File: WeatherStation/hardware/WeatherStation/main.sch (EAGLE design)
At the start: 38 parts, among them IC1 4017N, IC2 4017N

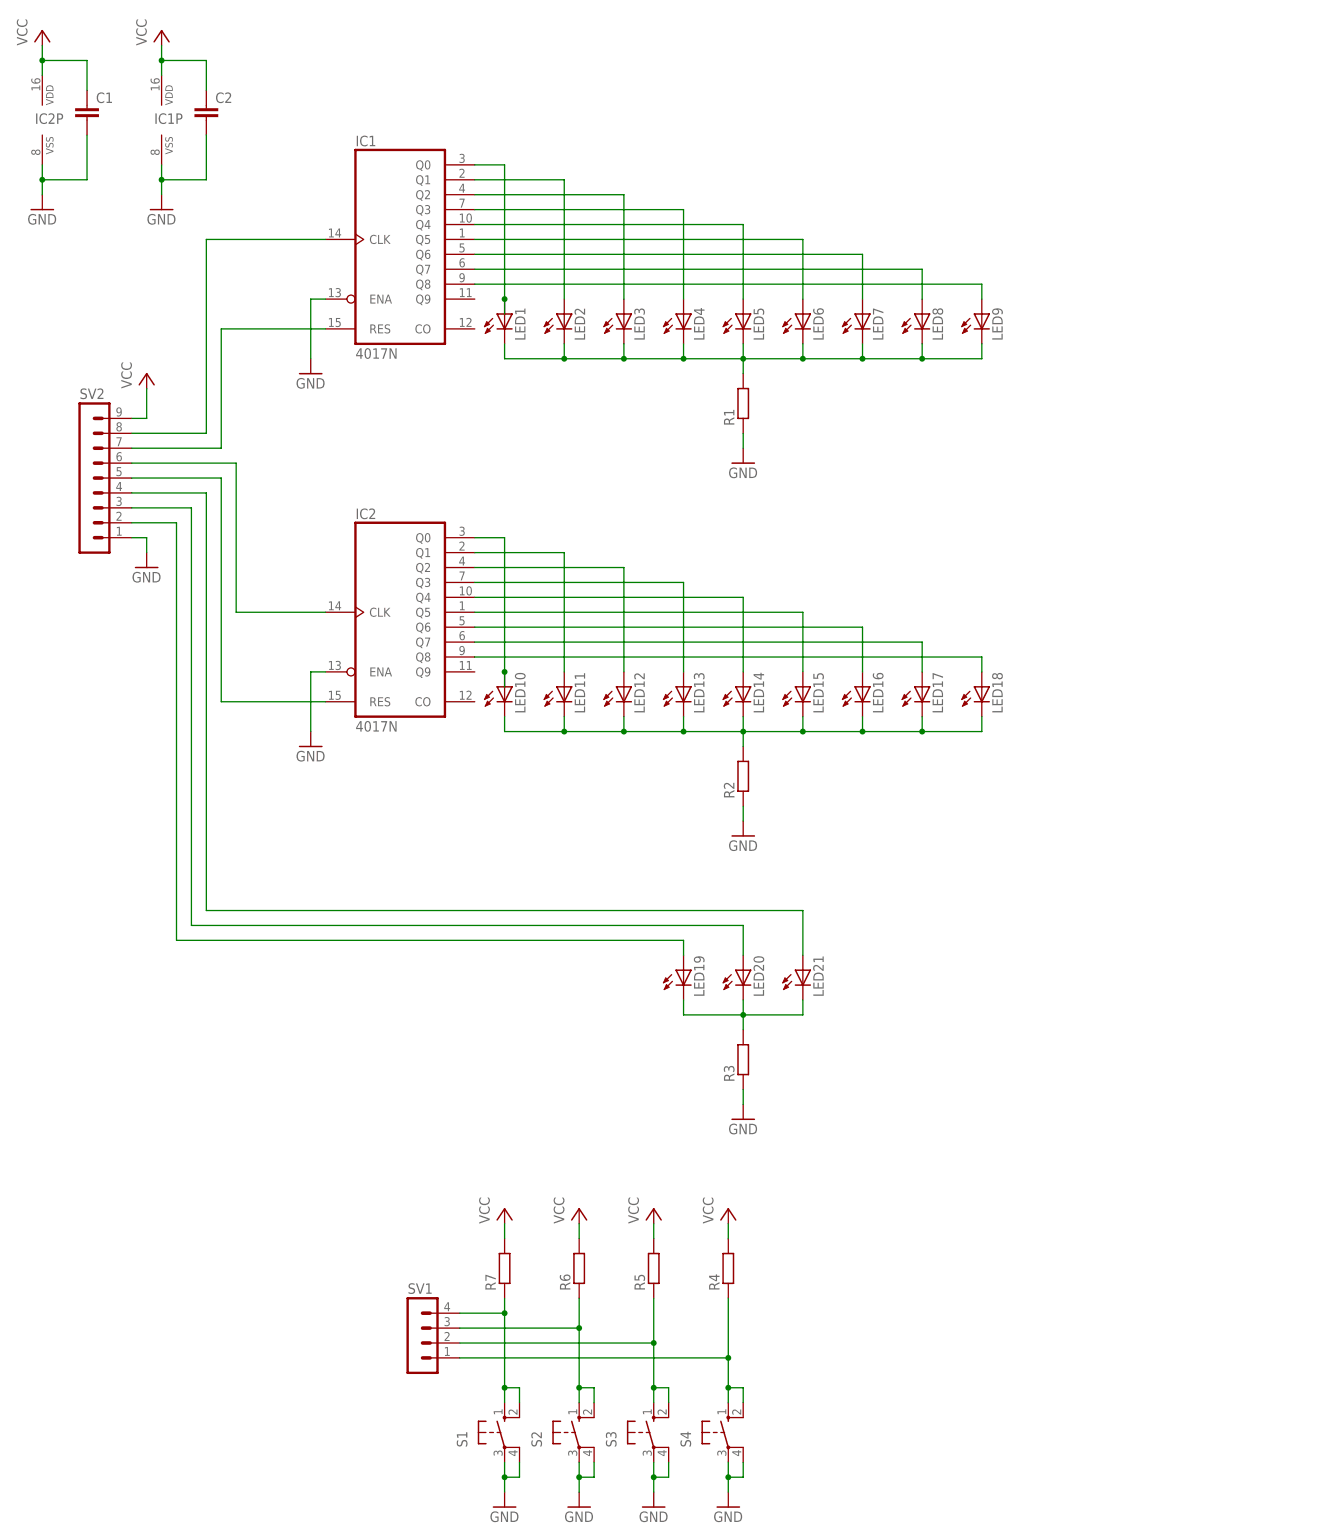
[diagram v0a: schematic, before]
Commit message: SCT2167 used as a LED driver.
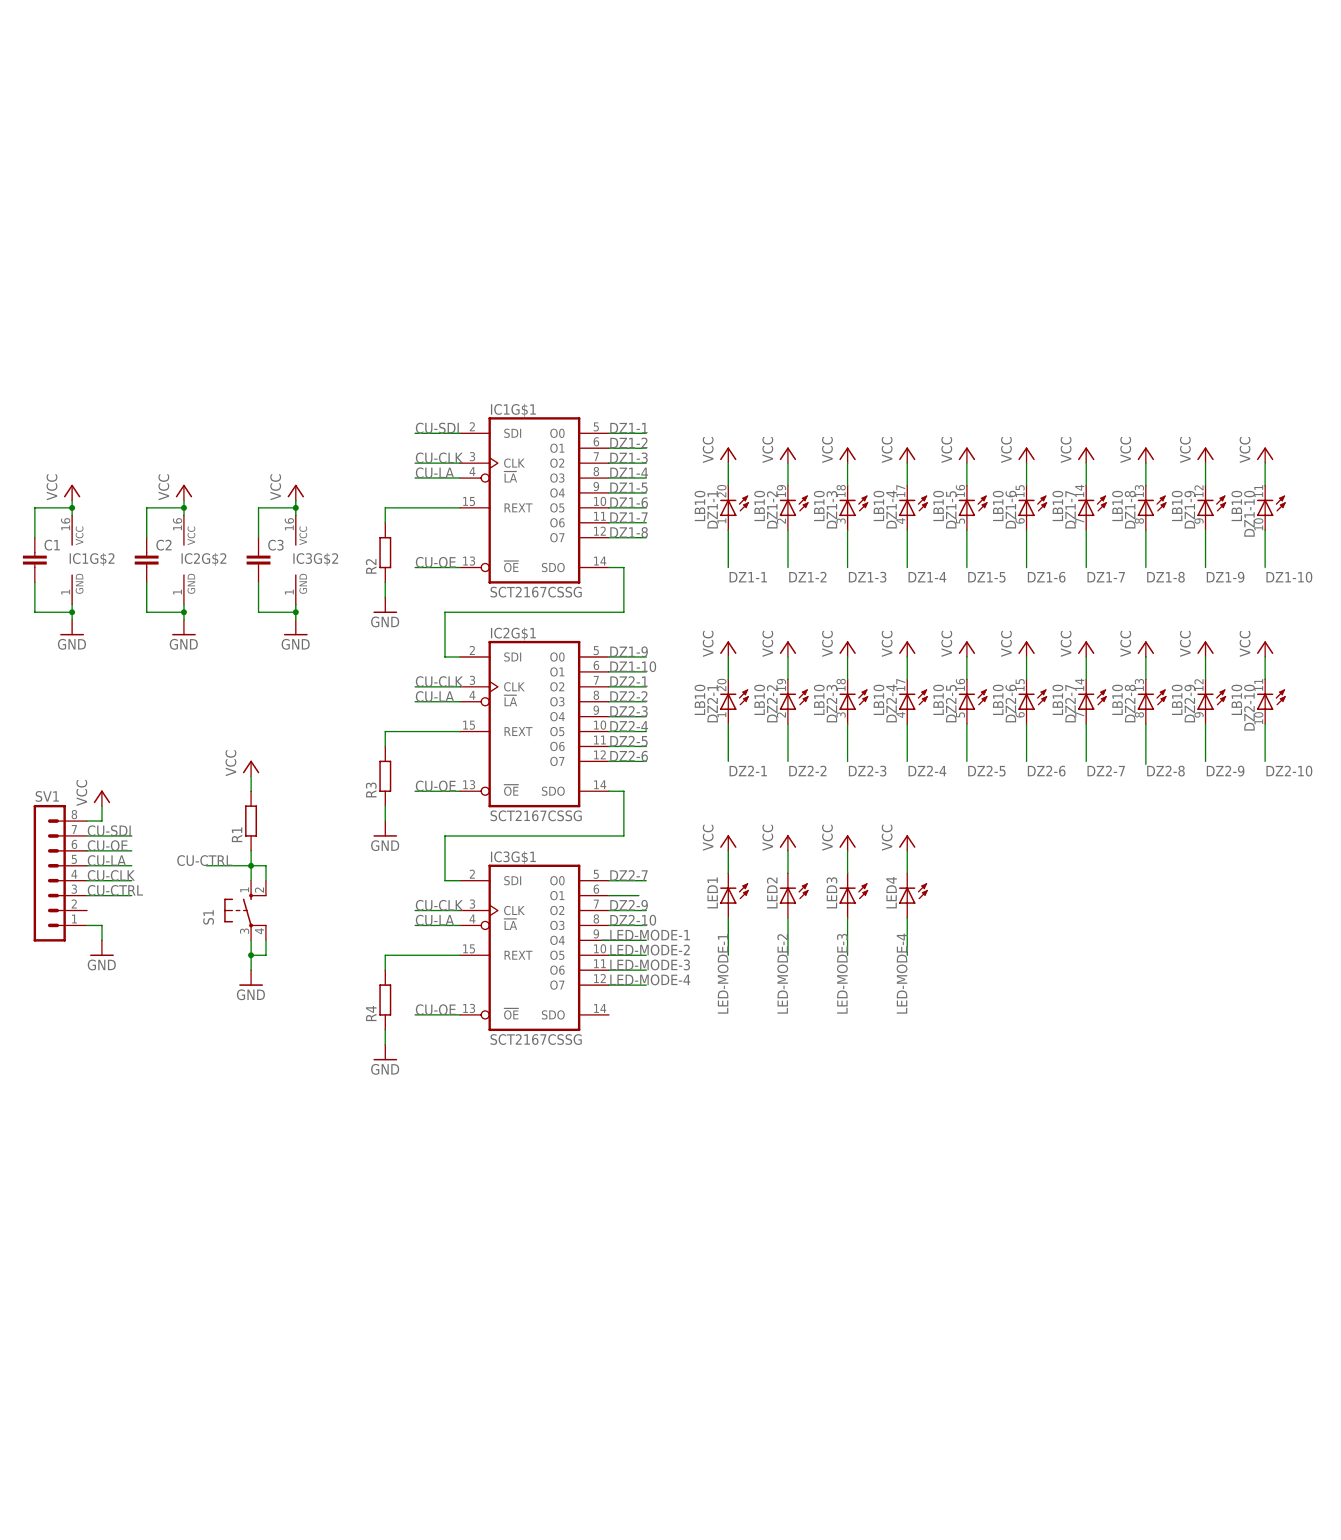
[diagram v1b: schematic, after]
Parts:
- removed LED10, LED11, LED12, LED13, LED14, LED15, LED16, LED17, LED18, LED19, LED20, LED21, LED5, LED6, LED7, LED8, LED9: (no value), led:LEDSML0603
- removed R5, R6, R7: (no value), resistor:R-EU_R1206
- removed S2, S3, S4: (no value), switch-omron:10-XX
- removed SV2: (no value), con-lstb:MA09-1
- added C3: (no value), resistor:C-EUC1206
- added DZ1, DZ2: LB10, led:LB10
- added IC3: SCT2167CSSG, starchips:SCT2167CSSG
- IC1, IC2: value 4017N -> SCT2167CSSG; device 40xx:4017N -> starchips:SCT2167CSSG
- LED1, LED2, LED3, LED4: device led:LEDSML0603 -> led:LED3MM
- SV1: device con-lstb:MA04-1 -> con-lstb:MA08-1
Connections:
- removed net N$1: LED1.C, LED2.C, LED3.C, LED4.C, LED5.C, LED6.C, LED7.C, LED8.C, LED9.C, R1.2
- removed net N$10: IC1A.Q8, LED9.A
- removed net N$11: LED10.C, LED11.C, LED12.C, LED13.C, LED14.C, LED15.C, LED16.C, LED17.C, LED18.C, R2.2
- removed net N$12: IC2A.Q0, LED10.A
- removed net N$14: IC2A.Q2, LED12.A
- removed net N$15: IC2A.Q3, LED13.A
- removed net N$16: IC2A.Q5, LED15.A
- removed net N$18: IC2A.Q7, LED17.A
- removed net N$19: IC2A.Q8, LED18.A
- removed net N$2: IC1A.Q0, LED1.A
- removed net N$20: IC2A.Q4, LED14.A
- removed net N$21: IC1A.CLK, SV2.8
- removed net N$22: IC1A.RES, SV2.7
- removed net N$23: LED19.C, LED20.C, LED21.C, R3.2
- removed net N$24: LED19.A, SV2.2
- removed net N$25: LED20.A, SV2.3
- removed net N$26: LED21.A, SV2.4
- removed net N$27: IC2A.RES, SV2.5
- removed net N$28: IC2A.CLK, SV2.6
- removed net N$29: R7.1, S1.S, S1.S1, SV1.4
- removed net N$30: R6.1, S2.S, S2.S1, SV1.3
- removed net N$31: R5.1, S3.S, S3.S1, SV1.2
- removed net N$32: R4.1, S4.S, S4.S1, SV1.1
- removed net N$5: IC1A.Q3, LED4.A
- removed net N$6: IC1A.Q4, LED5.A
- removed net N$7: IC1A.Q5, LED6.A
- removed net N$9: IC1A.Q7, LED8.A
- new net CU-CLK: IC1G$1.CLK, IC2G$1.CLK, IC3G$1.CLK, SV1.4
- new net CU-CTRL: R1.1, S1.S, S1.S1, SV1.3
- new net CU-LA: IC1G$1.!LA, IC2G$1.!LA, IC3G$1.!LA, SV1.5
- new net CU-OE: IC1G$1.!OE, IC2G$1.!OE, IC3G$1.!OE, SV1.6
- new net CU-SDI: IC1G$1.SDI, SV1.7
- new net DZ1-1: DZ1-1.A, IC1G$1.O0
- new net DZ1-10: DZ1-10.A, IC2G$1.O1
- new net DZ1-2: DZ1-2.A, IC1G$1.O1
- new net DZ1-3: DZ1-3.A, IC1G$1.O2
- new net DZ1-4: DZ1-4.A, IC1G$1.O3
- new net DZ1-5: DZ1-5.A, IC1G$1.O4
- new net DZ1-6: DZ1-6.A, IC1G$1.O5
- new net DZ1-7: DZ1-7.A, IC1G$1.O6
- new net DZ1-8: DZ1-8.A, IC1G$1.O7
- new net DZ1-9: DZ1-9.A, IC2G$1.O0
- new net DZ2-1: DZ2-1.A, IC2G$1.O2
- new net DZ2-10: DZ2-10.A, IC3G$1.O3
- new net DZ2-2: DZ2-2.A, IC2G$1.O3
- new net DZ2-3: DZ2-3.A, IC2G$1.O4
- new net DZ2-4: DZ2-4.A, IC2G$1.O5
- new net DZ2-5: DZ2-5.A, IC2G$1.O6
- new net DZ2-6: DZ2-6.A, IC2G$1.O7
- new net DZ2-7: DZ2-7.A, IC3G$1.O0
- new net DZ2-8: DZ2-8.A, IC3G$1.O1
- new net DZ2-9: DZ2-9.A, IC3G$1.O2
- new net LED-MODE-1: LED1.A
- new net LED-MODE-2: IC3G$1.O5, LED2.A
- new net LED-MODE-3: IC3G$1.O6, LED3.A
- new net LED-MODE-4: IC3G$1.O7, LED4.A
- net GND: now also C3.2, IC1G$2.GND, IC2G$2.GND, IC3G$2.GND, R4.1, SV1.1; no longer IC1A.ENA, IC1P.VSS, IC2A.ENA, IC2P.VSS, R1.1, S2.P, S2.P1, S3.P, S3.P1, S4.P, S4.P1, SV2.1
- net N$13: now also IC2G$1.REXT, R3.2; no longer IC2A.Q1, LED11.A
- net N$17: now also IC3G$1.REXT, R4.2; no longer IC2A.Q6, LED16.A
- net N$3: now also IC1G$1.SDO, IC2G$1.SDI; no longer IC1A.Q1, LED2.A
- net N$4: now also IC2G$1.SDO, IC3G$1.SDI; no longer IC1A.Q2, LED3.A
- net N$8: now also IC1G$1.REXT, R2.2; no longer IC1A.Q6, LED7.A
- net VCC: now also C3.1, DZ1-1.C, DZ1-10.C, DZ1-2.C, DZ1-3.C, DZ1-4.C, DZ1-5.C, DZ1-6.C, DZ1-7.C, DZ1-8.C, DZ1-9.C, DZ2-1.C, DZ2-10.C, DZ2-2.C, DZ2-3.C, DZ2-4.C, DZ2-5.C, DZ2-6.C, DZ2-7.C, DZ2-8.C, DZ2-9.C, IC1G$2.VCC, IC2G$2.VCC, IC3G$2.VCC, LED1.C, LED2.C, LED3.C, LED4.C, R1.2, SV1.8; no longer IC1P.VDD, IC2P.VDD, R4.2, R5.2, R6.2, R7.2, SV2.9
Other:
- moved on the sheet: C1, C2, LED1, LED2, LED3, LED4, R1, R2, R3, R4, S1
